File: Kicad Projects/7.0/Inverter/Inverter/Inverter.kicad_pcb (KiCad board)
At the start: 2 copper layers, 75 parts, among them IC1 1ED3322MC12NXUMA1, IC2 B0505S-2W, IC3 B0505S-2W, IC4 B0505S-2W, IC5 1ED3322MC12NXUMA1, J1 Conn_01x02_Male, J2 Conn_01x07_Male, J3 Conn_01x02_Male, U1 LM7809_TO220, U2 LM7809_TO220, U3 LM7809_TO220, U4 AMS1117-5.0, U5 AMS1117-5.0, U6 AMS1117-5.0, U7 FF300R12KS4, U8 AMS1117-3.3

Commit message: Inverter PCB Done
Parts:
- removed C29: 56uF, Capacitor_THT:CP_Radial_D16.0mm_P7.50mm
- removed C3, C4: 1000uF, 25V 1000uf:CAP_EEEFK1E102AQ
- added D10: Blue, LED_SMD:LED_0805_2012Metric_Pad1.15x1.40mm_HandSolder, B.Cu at (76.8, 150.0)
- added D11: Blue, LED_SMD:LED_0805_2012Metric_Pad1.15x1.40mm_HandSolder, B.Cu at (76.8, 148.0)
- added D12: Red, LED_SMD:LED_0805_2012Metric_Pad1.15x1.40mm_HandSolder, B.Cu at (42.5, 140.3)
- added D13: Red, LED_SMD:LED_0805_2012Metric_Pad1.15x1.40mm_HandSolder, B.Cu at (42.5, 142.8)
- added D14: Green, LED_SMD:LED_0805_2012Metric_Pad1.15x1.40mm_HandSolder, F.Cu at (34.0, 132.7)
- added D15: Green, LED_SMD:LED_0805_2012Metric_Pad1.15x1.40mm_HandSolder, F.Cu at (39.6, 132.7)
- added D16: Green, LED_SMD:LED_0805_2012Metric_Pad1.15x1.40mm_HandSolder, B.Cu at (85.6, 142.3)
- added D17: Green, LED_SMD:LED_0805_2012Metric_Pad1.15x1.40mm_HandSolder, B.Cu at (91.1, 142.3)
- added D18: Green, LED_SMD:LED_0805_2012Metric_Pad1.15x1.40mm_HandSolder, B.Cu at (42.3, 76.1)
- added D19: Green, LED_SMD:LED_0805_2012Metric_Pad1.15x1.40mm_HandSolder, F.Cu at (45.3, 149.9)
- added D9: Blue, LED_SMD:LED_0805_2012Metric_Pad1.15x1.40mm_HandSolder, B.Cu at (76.8, 152.0)
- added J4: Output Selector, Connector_PinSocket_1.27mm:PinSocket_1x03_P1.27mm_Vertical, B.Cu at (59.5, 148.7)
- added Q1: FS8205, 8205a:SOT95P280X145-6N, F.Cu at (43.0, 140.8)
- added Q2: FS8205, 8205a:SOT95P280X145-6N, F.Cu at (43.1, 144.3)
- added R11: 1.4, Resistor_SMD:R_0805_2012Metric_Pad1.20x1.40mm_HandSolder, F.Cu at (53.7, 129.2)
- added R12: 1.4, Resistor_SMD:R_0805_2012Metric_Pad1.20x1.40mm_HandSolder, F.Cu at (69.3, 129.3)
- added R13: 22K, Resistor_SMD:R_1206_3216Metric_Pad1.30x1.75mm_HandSolder, B.Cu at (44.9, 81.9)
- added R14: 22K, Resistor_SMD:R_1206_3216Metric_Pad1.30x1.75mm_HandSolder, B.Cu at (49.6, 76.8)
- added R15: 22K, Resistor_SMD:R_1206_3216Metric_Pad1.30x1.75mm_HandSolder, B.Cu at (47.2, 76.8)
- added R16: 22K, Resistor_SMD:R_1206_3216Metric_Pad1.30x1.75mm_HandSolder, B.Cu at (49.6, 81.9)
- added R17: 22K, Resistor_SMD:R_1206_3216Metric_Pad1.30x1.75mm_HandSolder, B.Cu at (44.8, 76.8)
- added R18: 470, Resistor_SMD:R_0603_1608Metric_Pad0.98x0.95mm_HandSolder, F.Cu at (77.0, 151.6)
- added R19: 470, Resistor_SMD:R_0603_1608Metric_Pad0.98x0.95mm_HandSolder, F.Cu at (77.0, 150.1)
- added R20: 470, Resistor_SMD:R_0603_1608Metric_Pad0.98x0.95mm_HandSolder, F.Cu at (77.0, 148.5)
- added R21: 470, Resistor_SMD:R_0603_1608Metric_Pad0.98x0.95mm_HandSolder, B.Cu at (38.9, 140.6)
- added R22: 470, Resistor_SMD:R_0603_1608Metric_Pad0.98x0.95mm_HandSolder, B.Cu at (38.9, 142.8)
- added R23: 3.3k, Resistor_SMD:R_0603_1608Metric_Pad0.98x0.95mm_HandSolder, F.Cu at (36.8, 133.9)
- added R24: 2.2k, Resistor_SMD:R_0603_1608Metric_Pad0.98x0.95mm_HandSolder, F.Cu at (36.8, 131.6)
- added R25: 2.2k, Resistor_SMD:R_0603_1608Metric_Pad0.98x0.95mm_HandSolder, B.Cu at (88.3, 143.4)
- added R26: 3.3k, Resistor_SMD:R_0603_1608Metric_Pad0.98x0.95mm_HandSolder, B.Cu at (88.3, 141.2)
- added R27: 470, Resistor_SMD:R_0603_1608Metric_Pad0.98x0.95mm_HandSolder, F.Cu at (43.5, 148.6)
- C11, C14, C16, C17, C18, C19, C21, C22, C26, C27, C28, C30, C31, C32, C33, C34, C35, C5, C6, C8, D1, D2, D4, D5, R10, R2, R7, R8, R9, U5, U6, U7, U8: moved to B.Cu
- R1, R3: value 3.3 -> 2.2
- moved H1 237.4 mm to (-129.3, 75.1)
- moved H2 237.4 mm to (-129.3, 83.1)
- moved H3 237.4 mm to (-129.3, 91.0)
- moved H4 237.4 mm to (-129.3, 99.0)
- moved C1 172.0 mm to (22.7, 162.4), turned to 180 degrees
- moved C5 161.6 mm to (24.0, 157.4), turned to -90 degrees
- moved C11 158.7 mm to (45.7, 157.5), turned to -90 degrees
- moved C2 156.8 mm to (46.8, 162.5), turned to 180 degrees
- moved C12 151.0 mm to (26.0, 137.3)
- moved C14 149.1 mm to (35.0, 148.8), turned to -90 degrees
- moved C15 143.0 mm to (41.4, 149.3), turned to -90 degrees
- moved C8 140.0 mm to (48.2, 157.5), turned to -90 degrees
- moved C19 138.8 mm to (56.0, 136.8)
- moved C7 137.0 mm to (72.9, 162.4), turned to 180 degrees
- moved C6 135.1 mm to (74.4, 157.5), turned to -90 degrees
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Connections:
- IC1 pad 4: unconnected-(IC1-NC-Pad4) -> Net-(IC1-OUT-)
- IC1 pad 7: unconnected-(IC1-CLAMP-Pad7) -> Net-(IC1-CLAMP)
- IC5 pad 4: unconnected-(IC5-NC-Pad4) -> Net-(IC5-OUT-)
- IC5 pad 7: unconnected-(IC5-CLAMP-Pad7) -> Net-(IC5-CLAMP)
- J2 pad 2: DIG5V -> Net-(J2-Pin_2)
- J3 pad 1: VAux+ -> VAux-
- J3 pad 2: VAux- -> VAux+
- R1 pad 2: Net-(R1-Pad2) -> Net-(IC1-CLAMP)
- R3 pad 2: Net-(R3-Pad2) -> Net-(IC5-CLAMP)
- R7 pad 2: -BATT -> Net-(R13-Pad2)
- U7 pad 4: Net-(R3-Pad2) -> Net-(IC5-CLAMP)
- U7 pad 6: Net-(R1-Pad2) -> Net-(IC1-CLAMP)
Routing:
- net RDY: track 0.00 -> 52.1 mm, vias 0 -> 4
- net FLT: track 0.00 -> 50.2 mm, vias 0 -> 4
- net RST: track 0.00 -> 41.3 mm, vias 0 -> 5
- net Net-(U6-VO): track 0.00 -> 33.9 mm, vias 0 -> 1
- net INLS: track 0.00 -> 33.3 mm, vias 0 -> 2
- net Net-(U5-VO): track 0.00 -> 33.2 mm, vias 0 -> 1
- net Net-(PS1-CTRL): track 0.00 -> 32.1 mm
- net VDrive2Neg: track 0.00 -> 31.0 mm, vias 0 -> 5
- net DIG-: track 0.00 -> 26.0 mm, vias 0 -> 3
- net VDrive1Neg: track 0.00 -> 23.4 mm, vias 0 -> 5
- net DIG+: track 0.00 -> 20.6 mm, vias 0 -> 7
- net Net-(IC5-CLAMP): track 0.00 -> 20.3 mm
- net Net-(IC1-CLAMP): track 0.00 -> 20.1 mm
- net +BATT: track 0.00 -> 19.5 mm, vias 0 -> 6
- net INHS: track 0.00 -> 18.4 mm, vias 0 -> 4
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- added copper zone on B.Cu, net +BATT
- added copper zone on F.Cu, net +BATT
- added copper zone on In1.Cu, net +BATT
- added copper zone on In2.Cu, net +BATT
- added copper zone on B.Cu, net -BATT
- added copper zone on F.Cu, net -BATT
- added copper zone on In1.Cu, net -BATT
- added copper zone on In2.Cu, net -BATT
- added copper zone on In2.Cu, net DIG+
- added copper zone on B.Cu, net DIG-
- added copper zone on F.Cu, net DIG-
- added copper zone on In1.Cu, net DIG5V
- added copper zone on B.Cu, net GND1
- added copper zone on F.Cu, net GND1
- added copper zone on B.Cu, net GND2
- added copper zone on F.Cu, net GND2
- added copper zone on B.Cu, net Net-(D7-K)
- added copper zone on F.Cu, net Net-(D7-K)
- added copper zone on In1.Cu, net Net-(D7-K)
- added copper zone on In2.Cu, net Net-(D7-K)
- added copper zone on B.Cu, net Net-(D8-A)
- added copper zone on F.Cu, net Net-(D8-A)
- added copper zone on In1.Cu, net Net-(D8-A)
- added copper zone on In2.Cu, net Net-(D8-A)
- added copper zone on B.Cu, net Net-(D8-K)
- added copper zone on F.Cu, net Net-(D8-K)
- added copper zone on In1.Cu, net Net-(D8-K)
- added copper zone on In2.Cu, net Net-(D8-K)
- added copper zone on B.Cu, net Net-(R13-Pad2)
- added copper zone on In1.Cu, net VAux+
- added copper zone on In2.Cu, net VAux+
- added copper zone on B.Cu, net VAux-
- added copper zone on F.Cu, net VAux-
- added copper zone on In1.Cu, net VDrive1
- added copper zone on In2.Cu, net VDrive1Neg
- added copper zone on In1.Cu, net VDrive2
- added copper zone on In2.Cu, net VDrive2Neg
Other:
- board outline added: 80.2 x 151.3 mm
- copper layers 2 -> 4

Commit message: IDEK
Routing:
- net +BATT: track 19.5 -> 20.1 mm, vias 6 -> 0
- net -BATT: vias 4 -> 0
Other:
- outline, holes or cut-outs redrawn
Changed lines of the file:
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@@
     )
   )
+  (gr_rect (start 42.545 107.2388) (end 72.5678 110.9472)
+    (stroke (width 0.1) (type default)) (fill none) (layer "Edge.Cuts"))
+  (gr_rect (start 29.0068 139.6238) (end 30.1244 143.1798)
+    (stroke (width 0.1) (type default)) (fill none) (layer "Edge.Cuts"))
+  (gr_rect (start 14.1224 143.7386) (end 28.3718 144.8054)
+    (stroke (width 0.1) (type default)) (fill none) (layer "Edge.Cuts"))
   (gr_poly
     (pts
@@
     )
     (stroke (width 0.1) (type solid)) (fill none) (layer "Edge.Cuts"))
+  (gr_rect (start 81.407 152.7302) (end 91.6686 153.67)
+    (stroke (width 0.1) (type default)) (fill none) (layer "Edge.Cuts"))
+  (gr_rect (start 59.8678 127.3302) (end 61.1886 137.033)
+    (stroke (width 0.1) (type default)) (fill none) (layer "Edge.Cuts"))
+  (gr_rect (start 28.8544 145.9992) (end 30.2514 151.5872)
+    (stroke (width 0.1) (type default)) (fill none) (layer "Edge.Cuts"))
+  (gr_rect (start 14.5542 118.4402) (end 33.02 119.9642)
+    (stroke (width 0.1) (type default)) (fill none) (layer "Edge.Cuts"))
+  (gr_rect (start 78.7908 140.5636) (end 80.1624 151.2316)
+    (stroke (width 0.1) (type default)) (fill none) (layer "Edge.Cuts"))
+  (gr_rect (start 31.5468 152.4508) (end 74.8538 153.4668)
+    (stroke (width 0.1) (type default)) (fill none) (layer "Edge.Cuts"))
+  (gr_rect (start 30.734 137.9474) (end 78.5622 139.3444)
+    (stroke (width 0.1) (type default)) (fill none) (layer "Edge.Cuts"))
+  (gr_rect (start 56.896 112.5474) (end 60.9346 121.9454)
+    (stroke (width 0.1) (type default)) (fill none) (layer "Edge.Cuts"))
   (segment (start 24.2193 162.4076) (end 25.4052 162.4076) (width 0.2) (layer "F.Cu") (net 1))
   (segment (start 75.8496 162.3953) (end 77.2212 161.0237) (width 0.2) (layer "F.Cu") (net 1))
@@
   (segment (start 76.581 133.6548) (end 75.5396 134.6962) (width 0.25) (layer "B.Cu") (net 19))
   (segment (start 76.2254 134.0104) (end 75.5396 134.6962) (width 0.25) (layer "B.Cu") (net 19))
-  (via micro (at 58.0136 79.4512) (size 0.8) (drill 0.4) (layers "In1.Cu" "B.Cu") (remove_unused_layers) (keep_end_layers) (zone_layer_connections "In2.Cu") (net 23))
-  (via micro (at 42.3164 77.7494) (size 0.8) (drill 0.4) (layers "In1.Cu" "B.Cu") (remove_unused_layers) (keep_end_layers) (zone_layer_connections "In2.Cu") (net 23))
-  (via micro (at 64.6938 79.3242) (size 0.8) (drill 0.4) (layers "In1.Cu" "B.Cu") (remove_unused_layers) (keep_end_layers) (zone_layer_connections "In2.Cu") (net 23))
-  (via micro (at 61.3664 79.4004) (size 0.8) (drill 0.4) (layers "In1.Cu" "B.Cu") (remove_unused_layers) (keep_end_layers) (zone_layer_connections "In2.Cu") (net 23))
   (segment (start 73.9775 107.3785) (end 73.787 107.188) (width 0.25) (layer "F.Cu") (net 24))
-  (segment (start 78.0542 123.1284) (end 77.6358 122.71) (width 0.25) (layer "F.Cu") (net 24))
+  (segment (start 78.2066 113.038389) (end 78.2066 111.6076) (width 0.25) (layer "F.Cu") (net 24))
   (segment (start 73.9775 107.3785) (end 73.8124 107.2134) (width 0.25) (layer "F.Cu") (net 24))
   (segment (start 73.787 107.188) (end 73.787 105.664) (width 0.25) (layer "F.Cu") (net 24))
-  (segment (start 77.6358 122.71) (end 77.6358 111.0368) (width 0.25) (layer "F.Cu") (net 24))
-  (segment (start 77.6358 111.0368) (end 73.9775 107.3785) (width 0.25) (layer "F.Cu") (net 24))
-  (via micro (at 45.0342 83.9724) (size 0.8) (drill 0.4) (layers "In1.Cu" "B.Cu") (remove_unused_layers) (keep_end_layers) (free) (zone_layer_connections "In2.Cu") (net 24))
-  (via micro (at 49.6062 84.0486) (size 0.8) (drill 0.4) (layers "In1.Cu" "B.Cu") (remove_unused_layers) (keep_end_layers) (free) (zone_layer_connections "In2.Cu") (net 24))
-  (via micro (at 47.2694 84.0232) (size 0.8) (drill 0.4) (layers "In1.Cu" "B.Cu") (remove_unused_layers) (keep_end_layers) (free) (zone_layer_connections "In2.Cu") (net 24))
-  (via micro (at 61.3918 83.8454) (size 0.8) (drill 0.4) (layers "In1.Cu" "B.Cu") (remove_unused_layers) (keep_end_layers) (free) (zone_layer_connections "In2.Cu") (net 24))
-  (via micro (at 58.1152 83.8454) (size 0.8) (drill 0.4) (layers "In1.Cu" "B.Cu") (remove_unused_layers) (keep_end_layers) (free) (zone_layer_connections "In2.Cu") (net 24))
-  (via micro (at 64.77 83.8708) (size 0.8) (drill 0.4) (layers "In1.Cu" "B.Cu") (remove_unused_layers) (keep_end_layers) (free) (zone_layer_connections "In2.Cu") (net 24))
+  (segment (start 78.3082 122.8744) (end 78.3082 119.562811) (width 0.25) (layer "F.Cu") (net 24))
+  (segment (start 77.6358 118.890411) (end 77.6358 113.609189) (width 0.25) (layer "F.Cu") (net 24))
+  (segment (start 78.2066 111.6076) (end 73.9775 107.3785) (width 0.25) (layer "F.Cu") (net 24))
+  (segment (start 78.0542 123.1284) (end 78.3082 122.8744) (width 0.25) (layer "F.Cu") (net 24))
+  (segment (start 78.3082 119.562811) (end 77.6358 118.890411) (width 0.25) (layer "F.Cu") (net 24))
+  (segment (start 77.6358 113.609189) (end 78.2066 113.038389) (width 0.25) (layer "F.Cu") (net 24))
   (via (at 51.348 124.587) (size 0.8) (drill 0.4) (layers "F.Cu" "B.Cu") (net 25))
   (segment (start 53.4905 127.127) (end 53.4905 126.7295) (width 0.25) (layer "B.Cu") (net 25))

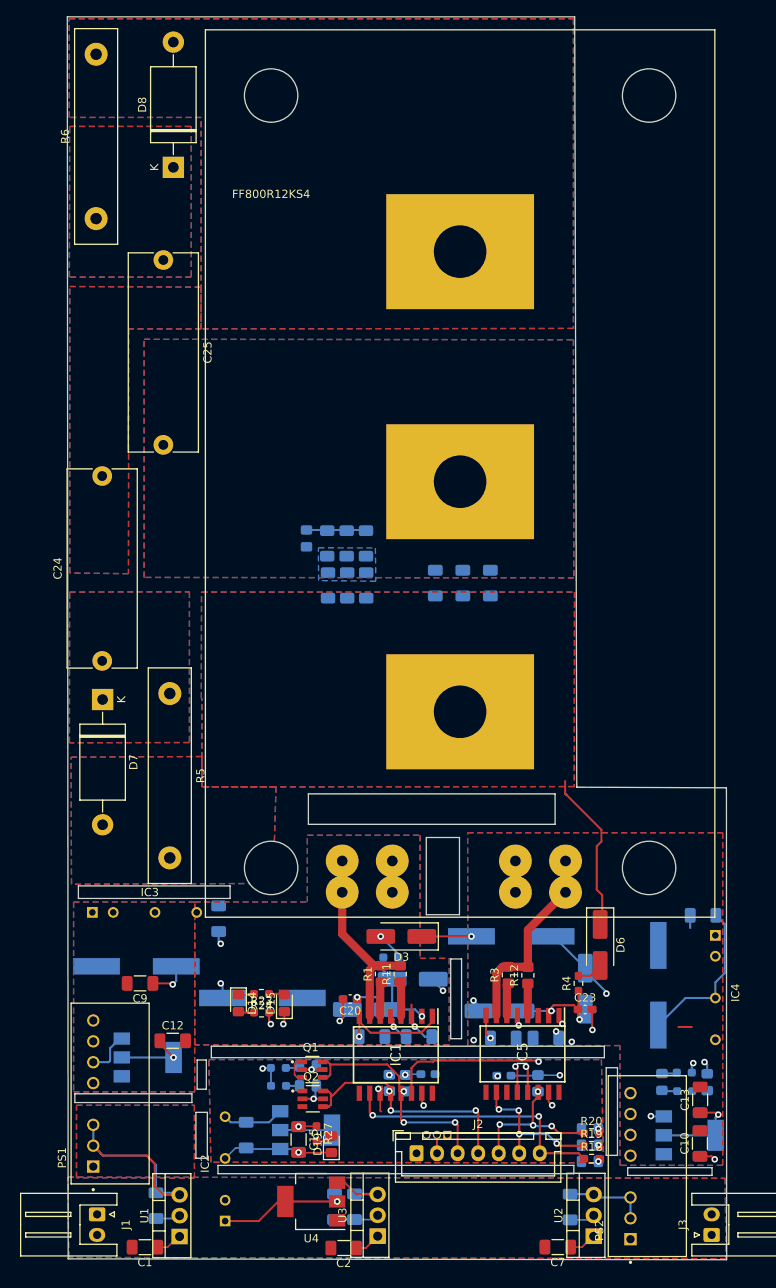
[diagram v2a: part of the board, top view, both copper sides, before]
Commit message: IDEK but LTC6804 Ordered
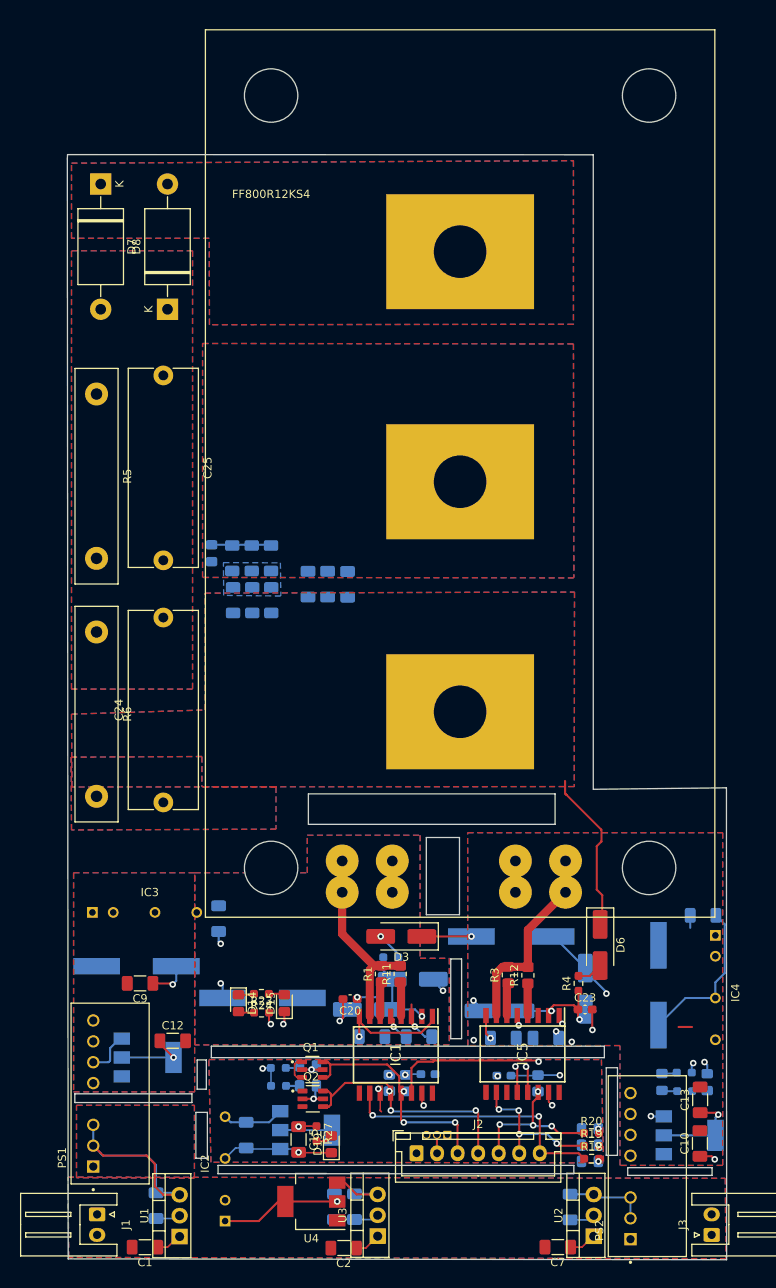
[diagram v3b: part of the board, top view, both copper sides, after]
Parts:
- moved D7 62.7 mm to (17.3, 33.0)
- moved R6 50.3 mm to (16.8, 87.5), turned to -90 degrees
- moved R5 37.5 mm to (16.8, 58.6)
- moved C24 18.8 mm to (24.9, 108.3)
- moved C26 17.4 mm to (47.3, 81.7)
- moved D8 17.3 mm to (25.4, 48.3)
- moved C27 16.5 mm to (44.9, 81.7)
- moved C28 15.5 mm to (42.5, 81.7)
- moved C25 14.0 mm to (24.9, 56.3)
- moved D18 11.7 mm to (30.8, 78.0)
- moved R14 11.7 mm to (38.0, 78.6)
- moved R15 11.7 mm to (35.6, 78.6)
- moved R17 11.7 mm to (33.3, 78.6)
- moved R13 11.7 mm to (33.4, 83.7)
- moved R16 11.7 mm to (38.0, 83.7)
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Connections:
- C24 pad 1: Net-(D7-K) -> +BATT
- C24 pad 2: Net-(D8-A) -> Net-(D7-A)
- D7 pad 2: +BATT -> Net-(D7-A)
- D8 pad 2: Net-(D8-A) -> Net-(D7-K)
- R5 pad 1: Net-(D7-K) -> -BATT
- R5 pad 2: +BATT -> Net-(D7-A)
- R6 pad 2: Net-(D8-A) -> +BATT
- U7 pad 1: Net-(D8-A) -> Net-(D7-K)
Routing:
- added copper zone on B.Cu, net Net-(D7-A)
- removed copper zone on B.Cu, net Net-(D8-A)
- removed copper zone on F.Cu, net Net-(D8-A)
- removed copper zone on In1.Cu, net Net-(D8-A)
- removed copper zone on In2.Cu, net Net-(D8-A)
- removed copper zone on B.Cu, net Net-(D8-K)
- removed copper zone on In1.Cu, net Net-(D8-K)
- removed copper zone on In2.Cu, net Net-(D8-K)
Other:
- board size 80.2 x 151.3 mm -> 80.2 x 134.5 mm

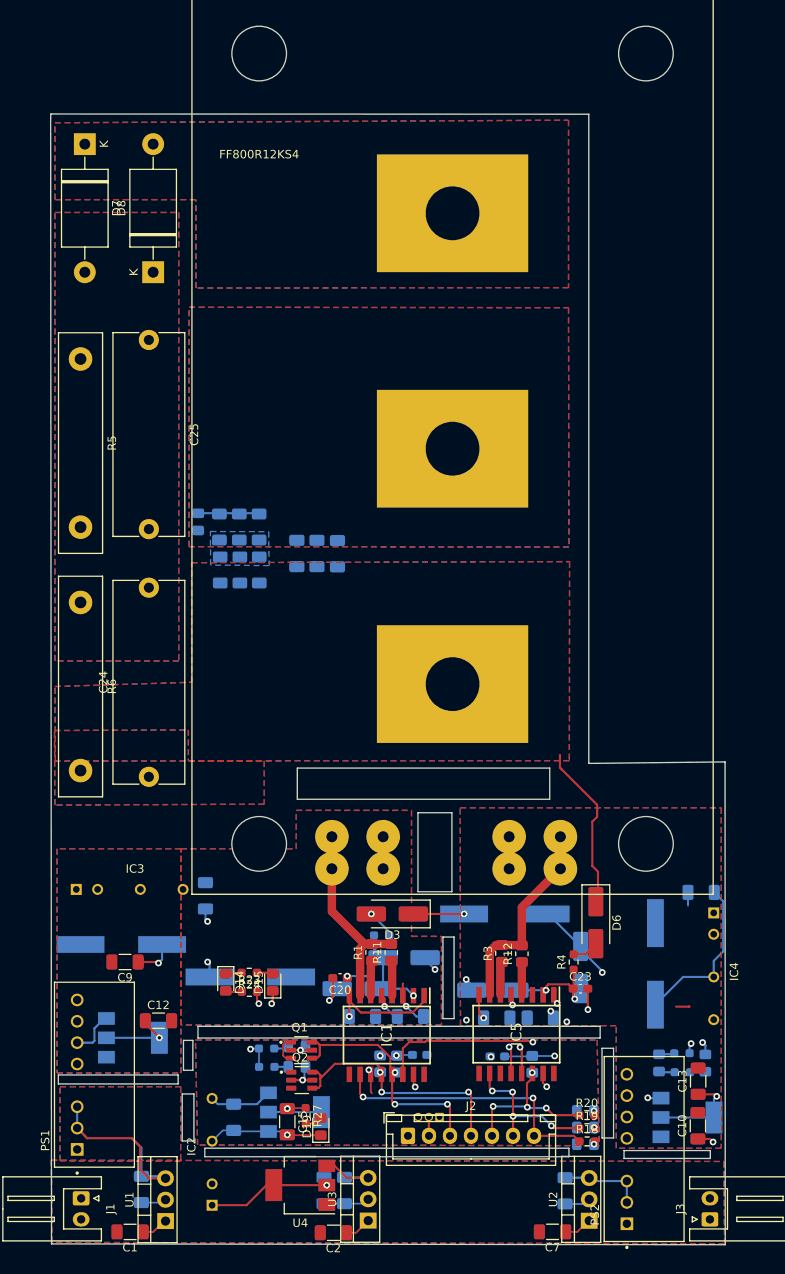
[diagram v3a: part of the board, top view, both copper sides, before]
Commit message: Inverter 0 errors ready to export, LU fucked
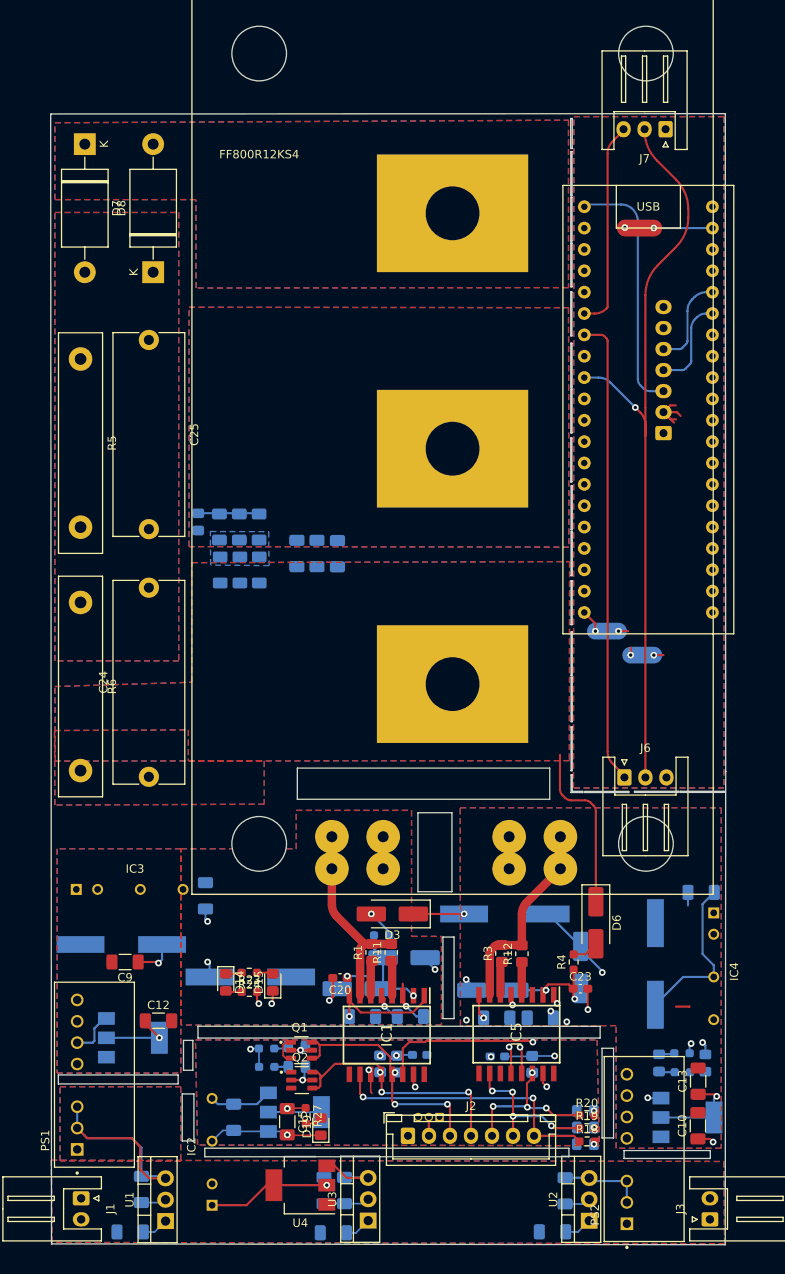
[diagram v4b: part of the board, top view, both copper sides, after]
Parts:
- added J5: Conn_01x07_Male, Connector_JST:JST_XH_B7B-XH-A_1x07_P2.50mm_Vertical, B.Cu at (86.1, 67.4)
- added J6: Conn_01x03_Pin, Connector_JST:JST_XH_S3B-XH-A_1x03_P2.50mm_Horizontal, F.Cu at (81.5, 108.3)
- added J7: Conn_01x03_Pin, Connector_JST:JST_XH_S3B-XH-A_1x03_P2.50mm_Horizontal, F.Cu at (86.3, 31.2)
- added U9: ChinaBluePill, Blue Pill:ChinaBluePill, F.Cu at (76.7, 88.7)
- C1, C2, C7: moved to B.Cu
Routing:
- net Net-(J6-Pin_2): track 0.00 -> 91.6 mm, vias 0 -> 1
- net Net-(J6-Pin_1): track 0.00 -> 55.9 mm
- net Net-(J5-Pin_3): track 0.00 -> 30.1 mm
- net Net-(J7-Pin_3): track 0.00 -> 24.9 mm
- net /3V3 MCU: track 0.00 -> 19.1 mm, vias 0 -> 4
- net Net-(J5-Pin_4): track 0.00 -> 11.2 mm
- net Net-(J5-Pin_5): track 0.00 -> 11.1 mm
- net /GND MCU: track 0.00 -> 10.4 mm, vias 0 -> 2
- net Net-(U6-VO): track 33.9 -> 35.2 mm
- net +BATT: track 20.1 -> 20.8 mm
- added copper zone on F.Cu, net /3V3 MCU
- added copper zone on B.Cu, net /GND MCU
- added copper zone on In1.Cu, net /OUTHS
- added copper zone on In2.Cu, net /OUTLS
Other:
- board size 80.2 x 134.5 mm -> 80.3 x 134.5 mm
